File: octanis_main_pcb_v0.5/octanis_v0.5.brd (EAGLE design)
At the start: 80 x 45 mm, 80 parts, among them IC1 BME280, IC2 BNO055A, Q1 32.768kHz, Q2 32.768kHz, U1 MSP432, U2 TPS61232, U3 DRV8836DSSR, U4 DRV8836DSSR, U5 DRV8836DSSR, U6 DRV8836DSSR, U7 SST25VF064C

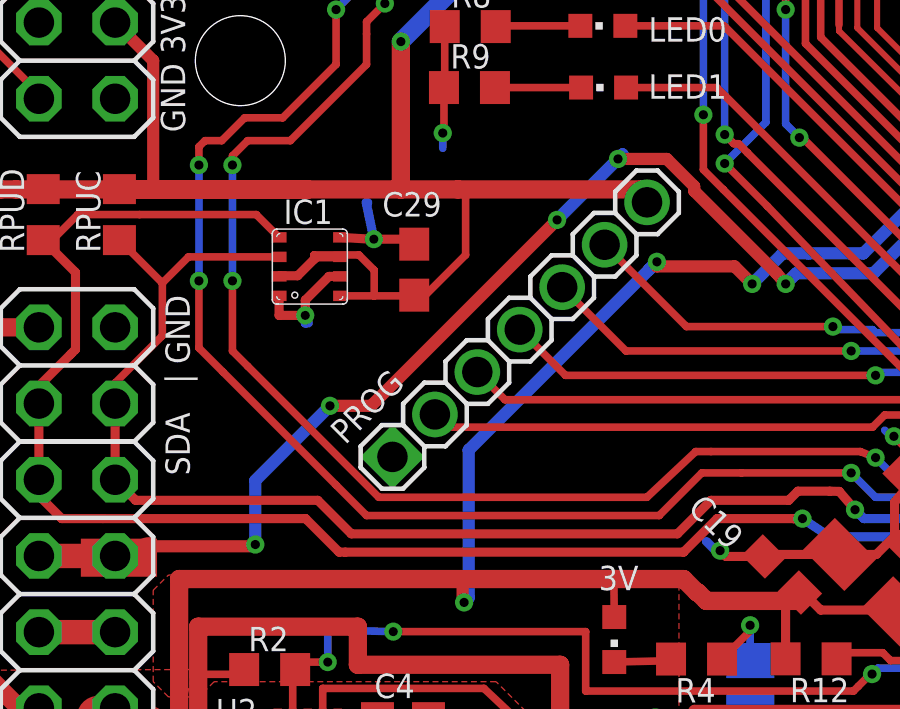
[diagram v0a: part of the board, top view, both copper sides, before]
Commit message: added RST pull-up
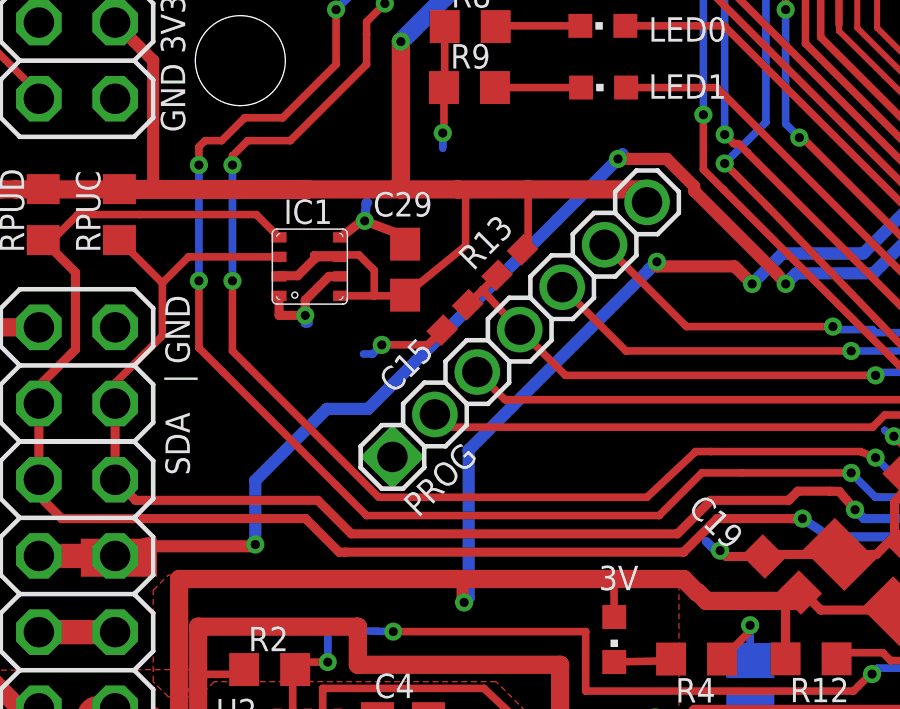
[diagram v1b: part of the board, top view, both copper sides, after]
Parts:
- added C15: 1n, rcl:0402
- added R13: 47k, rcl:0402
- moved C29 0.30 mm to (16.0, 24.1)
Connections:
- removed net N$75: PROG.4, U1.83
- new net RST_N: C15.1, PROG.4, R13.1, U1.83
- net +3V3: now also R13.2
- net GND: now also C15.2
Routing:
- net RST_N: track 0.00 -> 34.8 mm, vias 0 -> 4
- net N$75: track 31.6 -> 0.00 mm, vias 4 -> 0
- net GND: track 114.6 -> 117.4 mm, vias 32 -> 33
- net +3V3: track 375.8 -> 378.1 mm
- net AGND: vias 10 -> 8

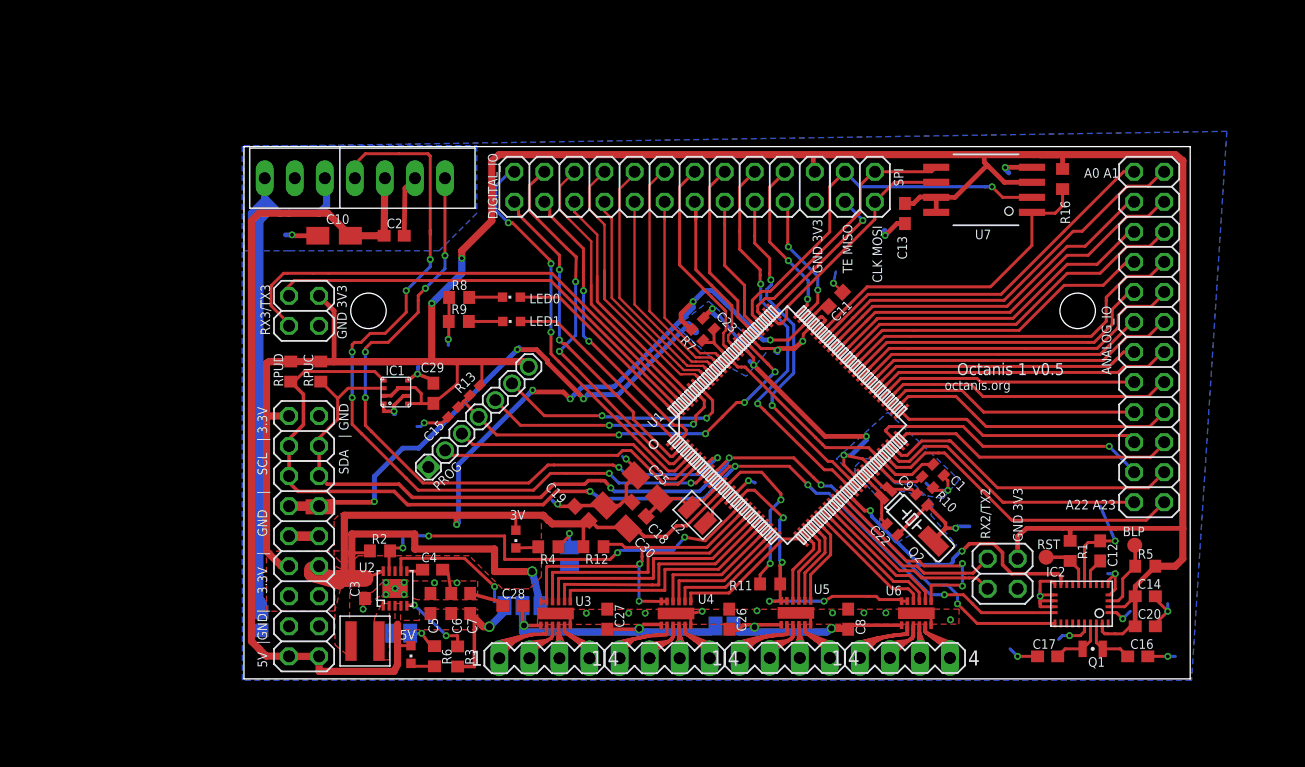
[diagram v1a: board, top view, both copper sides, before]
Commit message: added current sensors to motors on mainboard
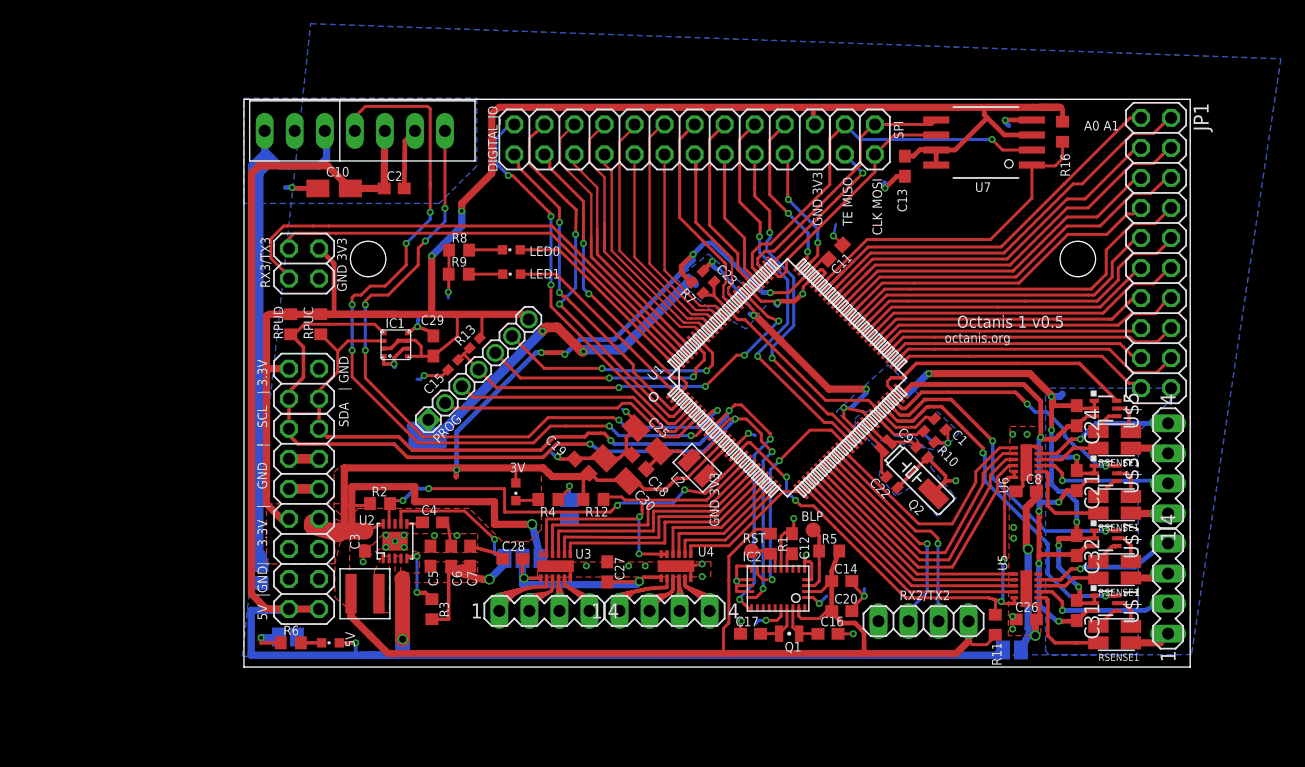
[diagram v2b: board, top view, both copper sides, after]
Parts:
- removed ANALOG_IO: (no value), pinhead:2X12
- added C21, C24, C31, C32: 10n, rcl:C0603
- added JP1: (no value), pinhead:2X10
- added R_SENSE1, R_SENSE2, R_SENSE3, R_SENSE5: RSENSE1, Octanis1_EPS:4PADS_RESISTOR
- added U$1, U$3, U$5, U$7: INA213, Octanis1_EPS:SC70-6
- RX2/TX2: device pinhead:2X02 -> pinhead:1X04
- moved SV3 32.9 mm to (78.1, 7.64), turned to 90 degrees
- moved SV4 27.4 mm to (78.1, 17.8), turned to 90 degrees
- moved BLP 27.2 mm to (48.1, 12.6)
- moved R5 26.8 mm to (49.5, 10.8)
- moved C16 26.3 mm to (49.4, 3.81)
- moved C12 26.1 mm to (46.3, 11.4)
- moved C14 25.7 mm to (50.5, 8.27)
- moved C20 25.7 mm to (50.5, 5.73)
- moved IC2 25.7 mm to (45.2, 7.64)
- moved Q1 25.7 mm to (46.1, 3.83)
- moved R1 25.4 mm to (44.5, 11.4)
- moved C17 25.2 mm to (42.8, 3.81)
- moved C26 25.1 mm to (66.1, 5.03), turned to 0 degrees
- moved RST 24.9 mm to (42.9, 10.8)
- moved MOT_J 24.4 mm to (64.9, 2.44)
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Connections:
- net AVCC1 renamed AVCC
- removed net A19: ANALOG_IO.20, U1.50
- removed net N$45 (its old number): SV3.1, U5.2
- removed net N$47: SV3.3, U5.4
- removed net N$53: SV4.1, U6.2
- removed net N$55: SV4.3, U6.4
- new net CURR_SENSE_EN: C21.2, C24.2, C31.2, C32.2, U$1.3, U$3.3, U$5.3, U$7.3, U1.50
- new net N$15: R_SENSE1.V2, U$1.5
- new net N$17: R_SENSE1.V1, U$1.4
- new net N$21: R_SENSE1.I2, SV3.1
- new net N$22: R_SENSE1.I1, U5.2
- new net N$23: R_SENSE5.V1, U$7.4
- new net N$24: R_SENSE5.V2, U$7.5
- new net N$25: R_SENSE5.I1, U5.4
- new net N$27: R_SENSE5.I2, SV3.3
- new net N$28: R_SENSE2.V2, U$3.5
- new net N$29: R_SENSE2.V1, U$3.4
- new net N$30: R_SENSE3.V2, U$5.5
- new net N$31: R_SENSE3.V1, U$5.4
- new net N$32: R_SENSE2.I2, SV4.1
- new net N$35: R_SENSE3.I1, U6.4
- new net N$36: R_SENSE2.I1, U6.2
- new net N$37: R_SENSE3.I2, SV4.3
- net +3V3: now also RX2/TX2.1; no longer RX2/TX2.3
- net +5V: now also MOT_J.2
- net A0: now also JP1.1; no longer ANALOG_IO.1
- net A1: now also JP1.2; no longer ANALOG_IO.2
- net A10: now also JP1.11; no longer ANALOG_IO.11
- net A11: now also JP1.12; no longer ANALOG_IO.12
- net A12: now also JP1.13; no longer ANALOG_IO.13
- net A13: now also JP1.14; no longer ANALOG_IO.14
- net A14: now also JP1.15; no longer ANALOG_IO.15
- net A15: now also JP1.16; no longer ANALOG_IO.16
- net A16: now also JP1.17; no longer ANALOG_IO.17
- net A17: now also JP1.18; no longer ANALOG_IO.18
- net A18: now also JP1.19; no longer ANALOG_IO.19
- net A2: now also JP1.3; no longer ANALOG_IO.3
- net A20: now also U$5.6; no longer ANALOG_IO.21
- net A21: now also U$3.6; no longer ANALOG_IO.22
- net A22: now also U$7.6; no longer ANALOG_IO.23
- net A23: now also U$1.6; no longer ANALOG_IO.24
- net A3: now also JP1.4; no longer ANALOG_IO.4
- net A4: now also JP1.5; no longer ANALOG_IO.5
- net A5: now also JP1.6; no longer ANALOG_IO.6
- net A6: now also JP1.7; no longer ANALOG_IO.7
- net A7: now also JP1.8; no longer ANALOG_IO.8
- net A8: now also JP1.9; no longer ANALOG_IO.9
- net A9: now also JP1.10; no longer ANALOG_IO.10
- net AGND: now also C21.1, C24.1, C31.1, C32.1, JP1.20, U$1.1, U$1.2, U$3.1, U$3.2, U$5.1, U$5.2, U$7.1, U$7.2
- net GND: now also RX2/TX2.4; no longer RX2/TX2.1
- net RX2: now also RX2/TX2.3; no longer RX2/TX2.2
- net TX2: now also RX2/TX2.2; no longer RX2/TX2.4
- net V_MOTOR: no longer MOT_J.2
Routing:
- net +5V: track 96.5 -> 168.6 mm, vias 2 -> 4
- net CURR_SENSE_EN: track 0.00 -> 55.6 mm, vias 0 -> 5
- net AGND: track 77.7 -> 116.2 mm, vias 8 -> 14
- net A19: track 23.8 -> 0.00 mm
- net M5678SLEEP: track 26.1 -> 44.4 mm
- net N$63: track 15.5 -> 0.00 mm
- net N$68: track 15.5 -> 0.00 mm
- net M5IN1: track 6.61 -> 21.3 mm
- net SCL: track 93.1 -> 79.1 mm
- net M5IN2: track 7.01 -> 20.9 mm
- net M7IN1: track 11.0 -> 24.9 mm
- net M6IN1: track 7.40 -> 20.5 mm
- net M7IN2: track 11.4 -> 24.3 mm
- net SDA: track 87.2 -> 74.5 mm
- net M6IN2: track 7.83 -> 20.1 mm
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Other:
- board size 80 x 45 mm -> 80 x 48 mm
- board text removed: "A22 A23"

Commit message: silkscreen ready
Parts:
- RS1: value RSENSE1 -> RS1
- RS2: value RSENSE1 -> RS2
- RS3: value RSENSE1 -> RS3
- RS4: value RSENSE1 -> RS4
- renumbered JP1 to ANALOG, R_SENSE1 to RS1, R_SENSE2 to RS3, R_SENSE3 to RS4, R_SENSE5 to RS2, U$1 to U8, U$3 to U10, U$5 to U11, U$7 to U9
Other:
- board text added: "A16 A17"
- board text added: "A18 AGND"

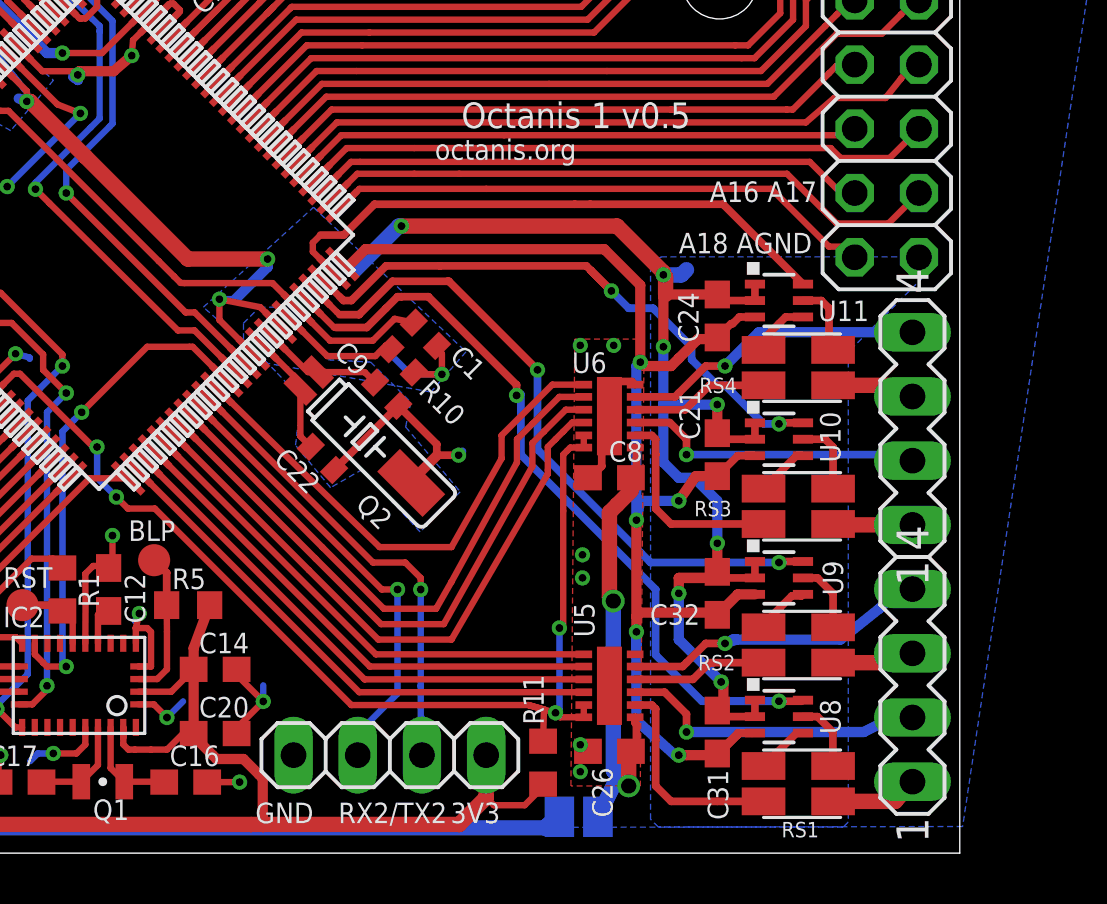
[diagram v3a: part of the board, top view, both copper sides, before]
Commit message: added Vref and low pass filters for current sensors to mainboard
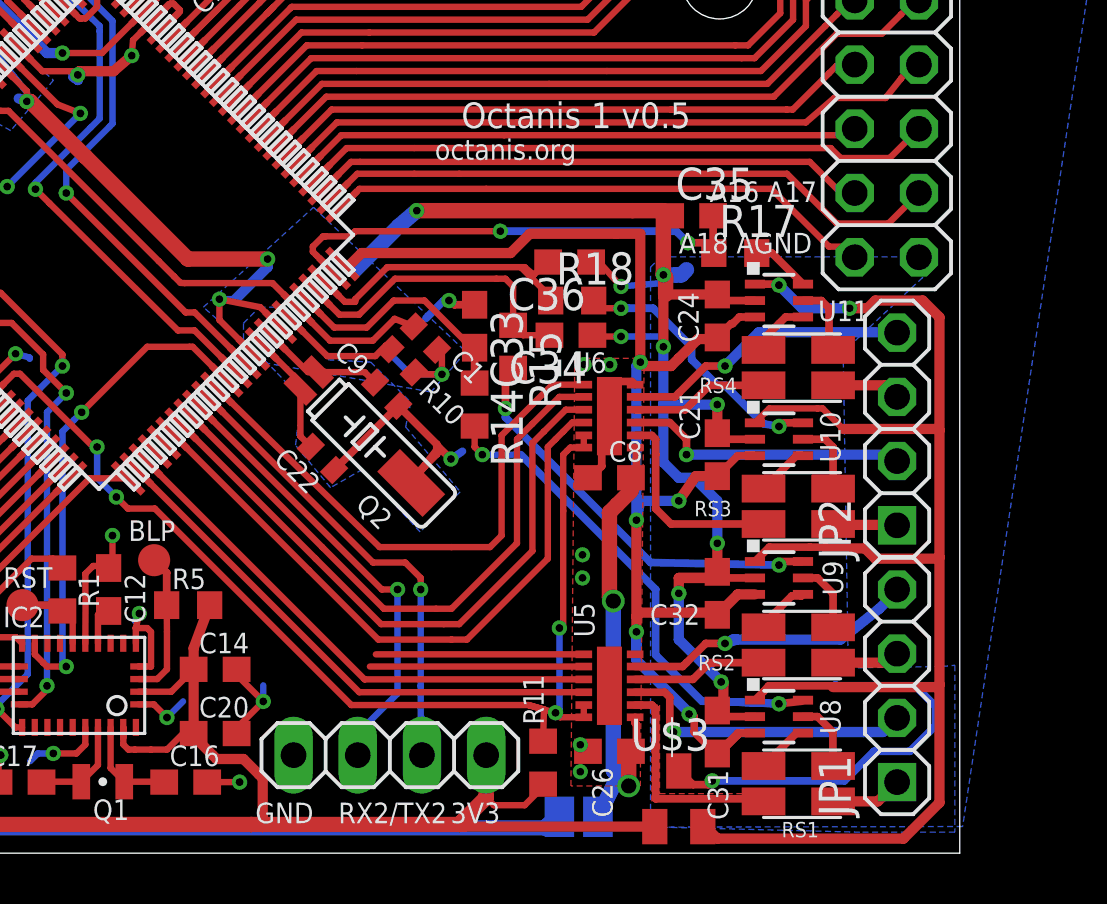
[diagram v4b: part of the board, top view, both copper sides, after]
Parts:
- removed SV3, SV4: (no value), con-lstb:MA04-1
- added C33, C34, C35, C36: 470n, rcl:C0603
- added JP1, JP2: (no value), pinhead-2:1X04-S
- added R14, R15, R17, R18: 6.8k, rcl:R0603
- added U$3: MAX6001SOT-23, Octanis1:MAX6001
- moved C1 0.15 mm to (58.9, 21.4)
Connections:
- net N$22 renamed M5OUT1
- new net A20UNF: R17.2, U11.6
- new net A21UNF: R18.2, U10.6
- new net A22UNF: R15.2, U9.6
- new net A23UNF: R14.2, U8.6
- new net VREF_M: U$3.2, U10.1, U11.1, U8.1, U9.1
- net +3V3: now also U$3.1
- net A20: now also C35.2, R17.1; no longer U11.6
- net A21: now also C36.2, R18.1; no longer U10.6
- net A22: now also C34.2, R15.1; no longer U9.6
- net A23: now also C33.2, R14.1; no longer U8.6
- net AGND: now also C33.1, C34.1, C35.1, C36.1, U$3.3; no longer U10.1, U11.1, U8.1, U9.1
- net M6IN1: now also U1.30; no longer U1.29
- net M6IN2: now also U1.29; no longer U1.30
- net N$21: now also JP1.1; no longer SV3.1
- net N$27: now also JP1.3; no longer SV3.3
- net N$32: now also JP2.1; no longer SV4.1
- net N$37: now also JP2.3; no longer SV4.3
- net N$38: now also JP1.2; no longer SV3.2
- net N$43: now also JP1.4; no longer SV3.4
- net N$45: now also JP2.4; no longer SV4.4
- net N$54: now also JP2.2; no longer SV4.2
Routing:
- net VREF_M: track 0.00 -> 60.8 mm, vias 0 -> 2
- net AGND: track 116.2 -> 141.9 mm, vias 14 -> 18
- net A23: track 33.0 -> 10.1 mm, vias 2 -> 0
- net A23UNF: track 0.00 -> 22.1 mm, vias 0 -> 2
- net A22UNF: track 0.00 -> 16.3 mm, vias 0 -> 2
- net A22: track 26.7 -> 12.1 mm, vias 2 -> 0
- net M6IN1: track 20.5 -> 8.46 mm
- net A21: track 23.8 -> 11.9 mm, vias 2 -> 0
- net M6IN2: track 20.1 -> 8.22 mm
- net A21UNF: track 0.00 -> 10.9 mm, vias 0 -> 2
- net +3V3: track 376.1 -> 383.9 mm
- net A20: track 22.9 -> 19.3 mm, vias 0 -> 2
- net A20UNF: track 0.00 -> 2.34 mm
- net M8IN2: track 20.8 -> 22.0 mm
- net M7IN1: track 24.9 -> 25.8 mm
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- added copper zone on layer 1, net M5OUT1

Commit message: finised revised mainboard
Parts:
- removed SV1, SV2: (no value), con-lstb:MA04-1
- added M1/M2, M3/M4: (no value), pinhead-2:1X04-S
- RX2/TX2: device pinhead:1X04 -> pinhead-2:1X04-S
- moved RX2/TX2 52.8 mm to (5.38, -4.06), turned to 0 degrees
- renumbered JP1 to M5/M6, JP2 to M7/M8, U$3 to U12
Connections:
- net N$13: now also M3/M4.1; no longer SV2.1
- net N$39: now also M3/M4.2; no longer SV2.2
- net N$40: now also M3/M4.3; no longer SV2.3
- net N$41: now also M3/M4.4; no longer SV2.4
- net N$49: now also M1/M2.1; no longer SV1.1
- net N$50: now also M1/M2.2; no longer SV1.2
- net N$51: now also M1/M2.3; no longer SV1.3
- net N$52: now also M1/M2.4; no longer SV1.4
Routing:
- net M6IN2: track 8.22 -> 21.2 mm, vias 0 -> 2
- net M6IN1: track 8.46 -> 20.6 mm
- net M5OUT1: track 8.74 -> 5.69 mm
- net N$49: track 15.5 -> 13.2 mm
- net N$52: track 8.02 -> 6.25 mm
- net N$51: track 8.17 -> 6.62 mm
- net N$13: track 5.74 -> 4.20 mm
- net N$50: track 7.67 -> 6.71 mm
- net N$41: track 3.89 -> 2.94 mm
- net TX2: track 18.9 -> 18.0 mm
- net +3V3: track 383.9 -> 383.1 mm
- net N$39: track 3.81 -> 3.10 mm
